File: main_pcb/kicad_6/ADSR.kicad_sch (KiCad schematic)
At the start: 25 parts, among them Q901 MMBT3904, U12 TL072, U13 LM555xM, U14 CD4052B

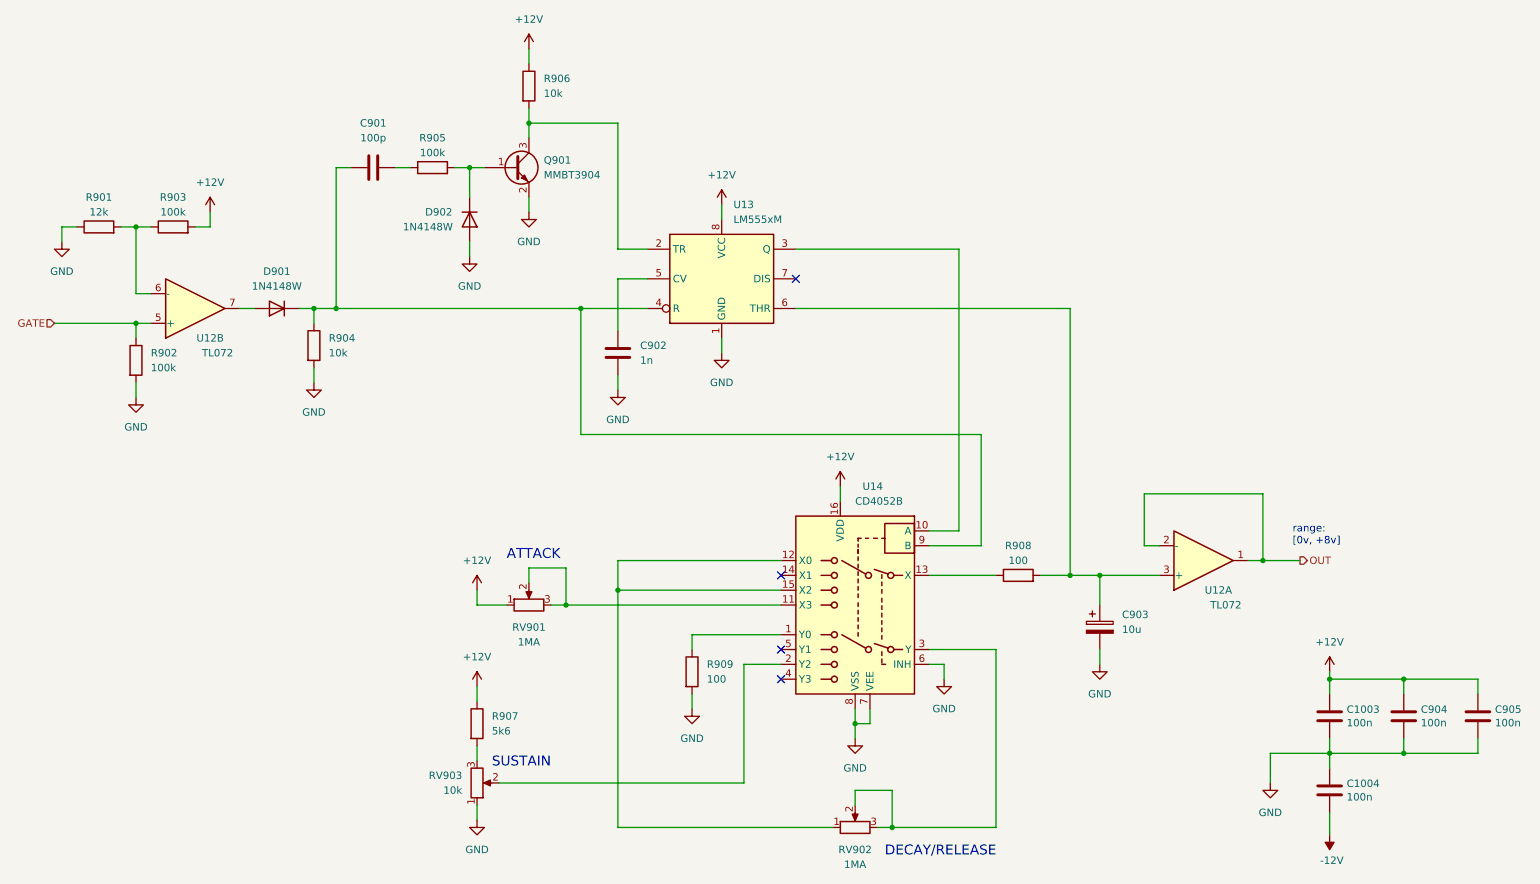
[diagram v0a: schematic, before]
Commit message: Update rev 0.1, fix VCA tails, add local 2v5 regs, change some pot footprints
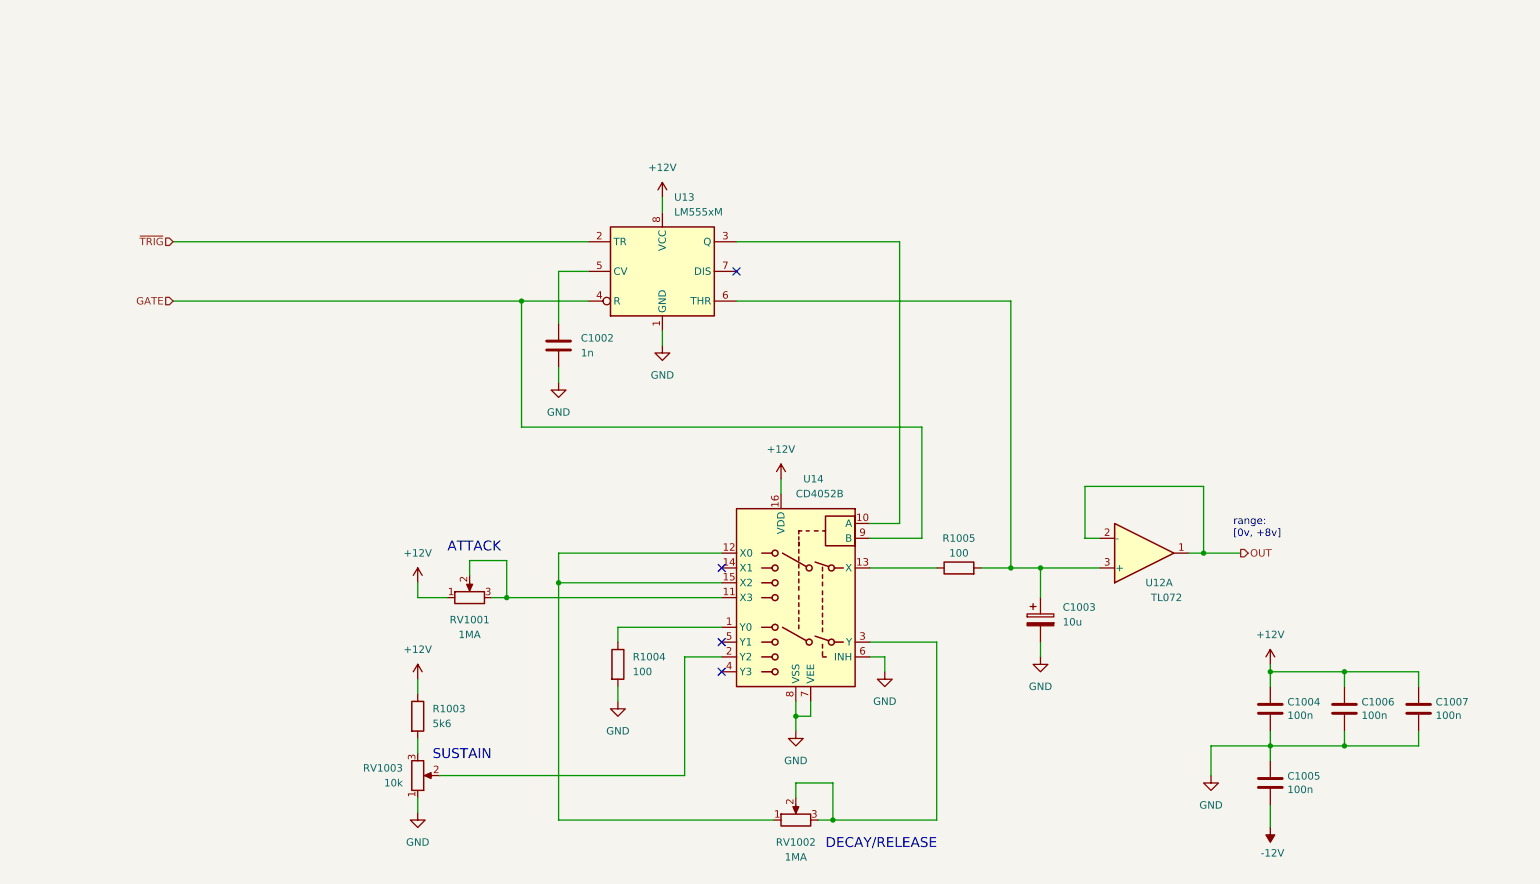
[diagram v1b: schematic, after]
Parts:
- removed C901: 100p, Capacitor_SMD:C_0603_1608Metric, symbol Device:C
- removed D901, D902: 1N4148W, Diode_SMD:D_SOD-123, symbol Diode:1N4148W
- removed Q901: MMBT3904, Package_TO_SOT_SMD:SOT-23, symbol Transistor_BJT:MMBT3904
- removed R901: 12k, Resistor_SMD:R_0603_1608Metric, symbol Device:R
- removed R902, R903, R905: 100k, Resistor_SMD:R_0603_1608Metric, symbol Device:R
- removed R904, R906: 10k, Resistor_SMD:R_0603_1608Metric, symbol Device:R
- removed unit 2 of U12
- renumbered C902 to C1002, C903 to C1003, C1003 to C1004, C1004 to C1005, C904 to C1006, C905 to C1007, R907 to R1003, R909 to R1004, R908 to R1005, RV901 to RV1001, RV902 to RV1002, RV903 to RV1003
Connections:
- net GATE: now also U13.4 (R), U14.9 (B)
- net ~{TRIG}: now reaches U13.2 (TR)
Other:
- moved on the sheet: C1002, C1003, C1004, C1005, C1006, C1007, R1003, R1004, R1005, RV1001, RV1002, RV1003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

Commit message: Change 555 timer type, fixes odd ADSR behavior
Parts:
- U13: value LM555xM -> TLC555
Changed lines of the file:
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@@
       (effects (font (size 1.27 1.27)) (justify left))
     )
-    (property "Value" "LM555xM" (id 1) (at 135.3694 52.07 0)
+    (property "Value" "TLC555" (id 1) (at 135.3694 52.07 0)
       (effects (font (size 1.27 1.27)) (justify left))
     )
@@
       (effects (font (size 1.27 1.27)) hide)
     )
-    (property "Datasheet" "http://www.ti.com/lit/ds/symlink/lm555.pdf" (id 3) (at 154.94 72.39 0)
+    (property "Datasheet" "" (id 3) (at 154.94 72.39 0)
       (effects (font (size 1.27 1.27)) hide)
     )

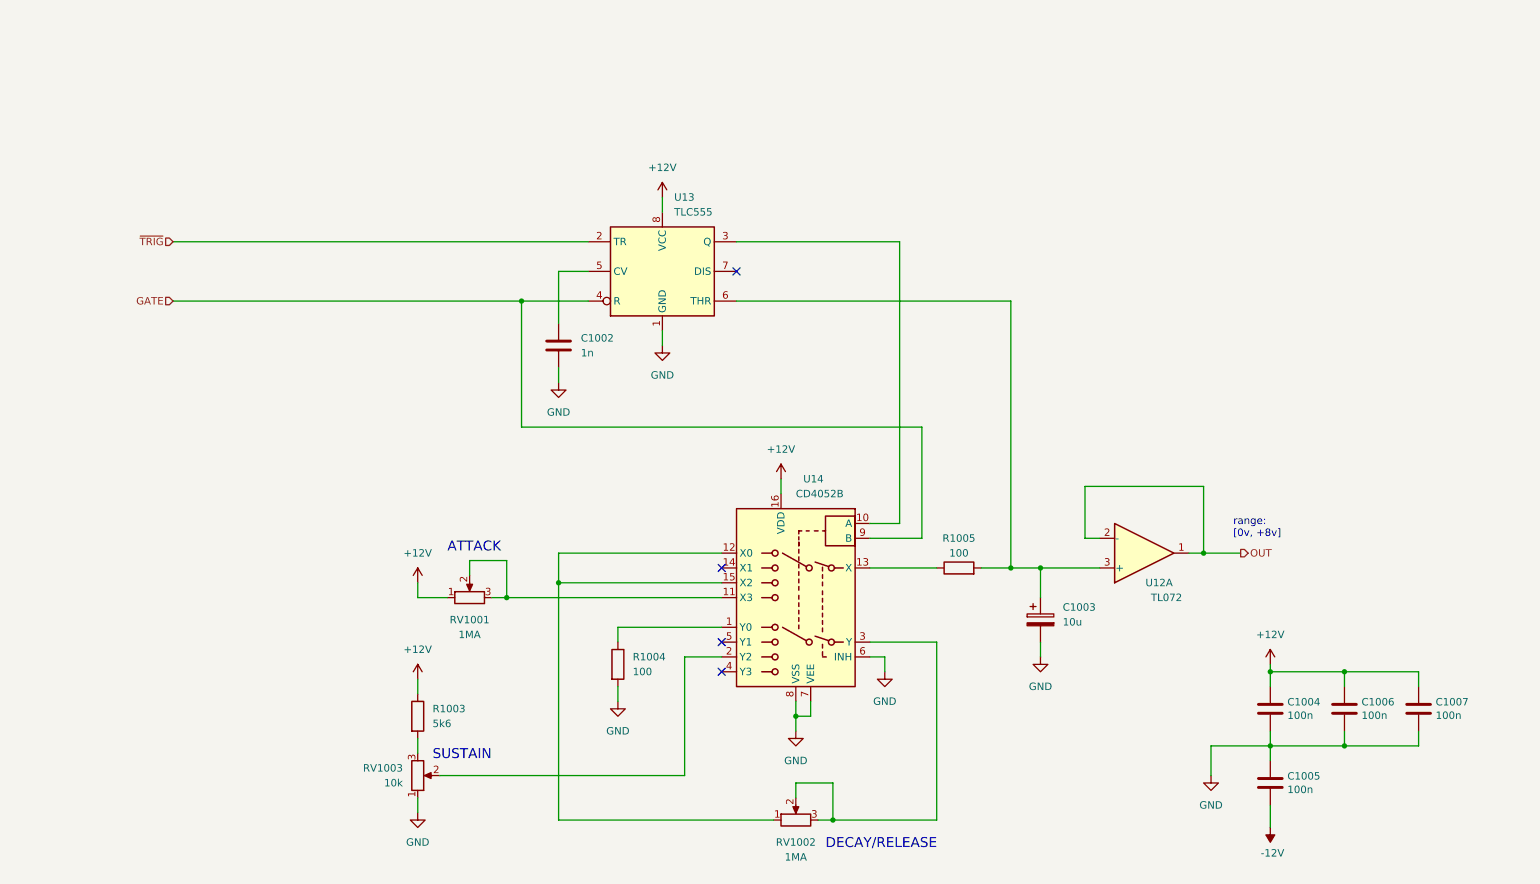
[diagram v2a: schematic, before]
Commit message: Add mod-wheel VCA, fix occasional VCO freq locking
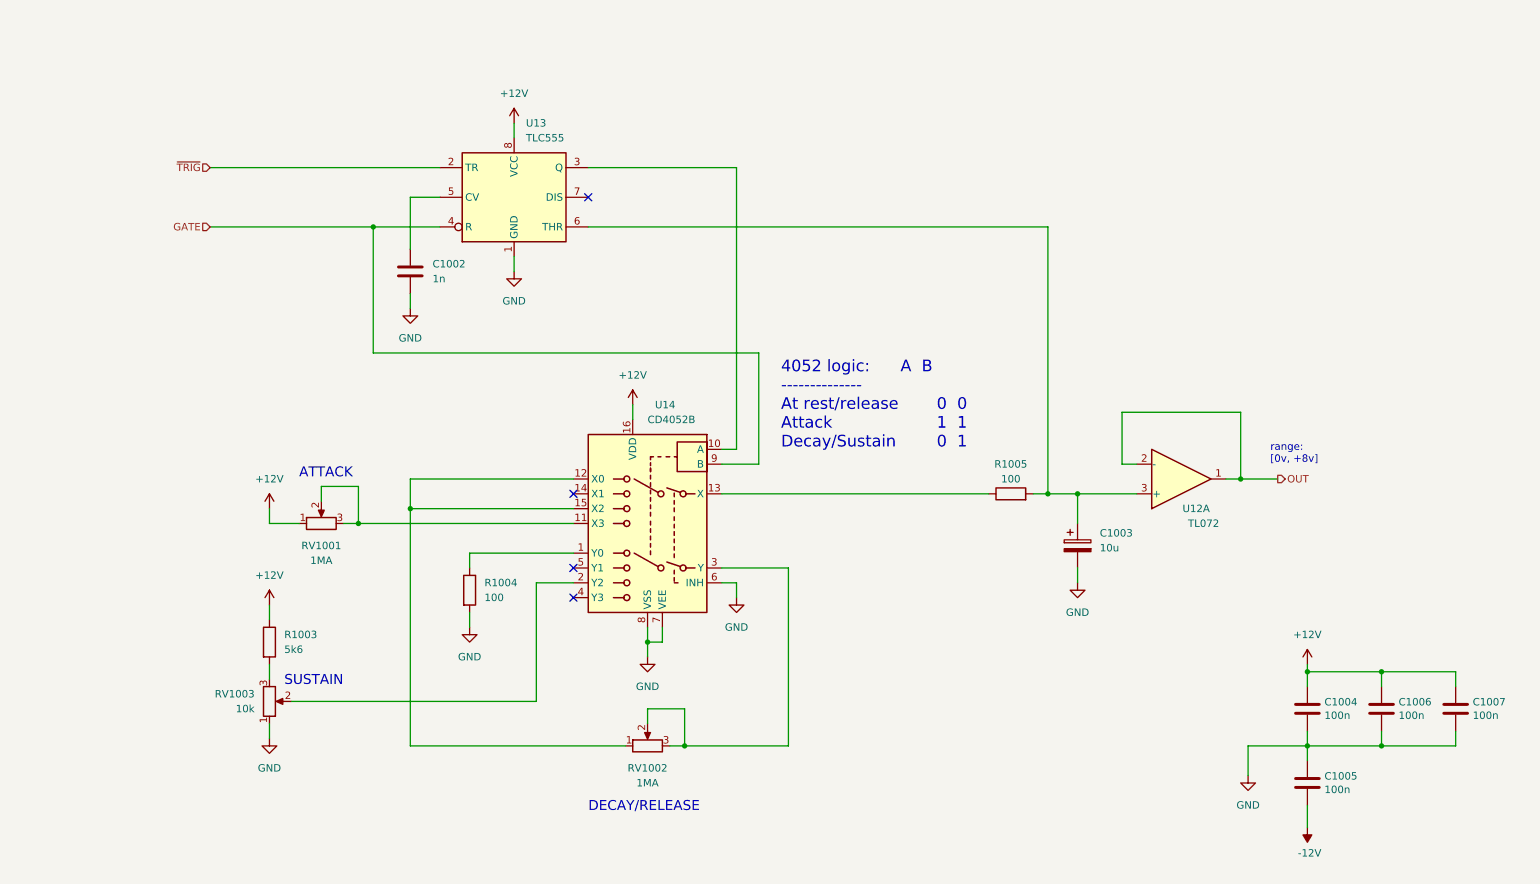
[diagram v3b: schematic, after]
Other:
- note added: "0 0 1 1 0 1"
- note added: "4052 logic: A B -------------- At rest/release Attack Decay/Sustain"
- moved on the sheet: C1002, C1003, C1004, C1005, C1006, C1007, R1003, R1004, R1005, RV1001, RV1002, RV1003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
